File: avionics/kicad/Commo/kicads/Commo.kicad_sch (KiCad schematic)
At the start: 84 parts, among them U1 ByA 100nF +3V3 U1-VDDA Bypass, U1 ByB 100nF +3V3 U1-VDD Bypass

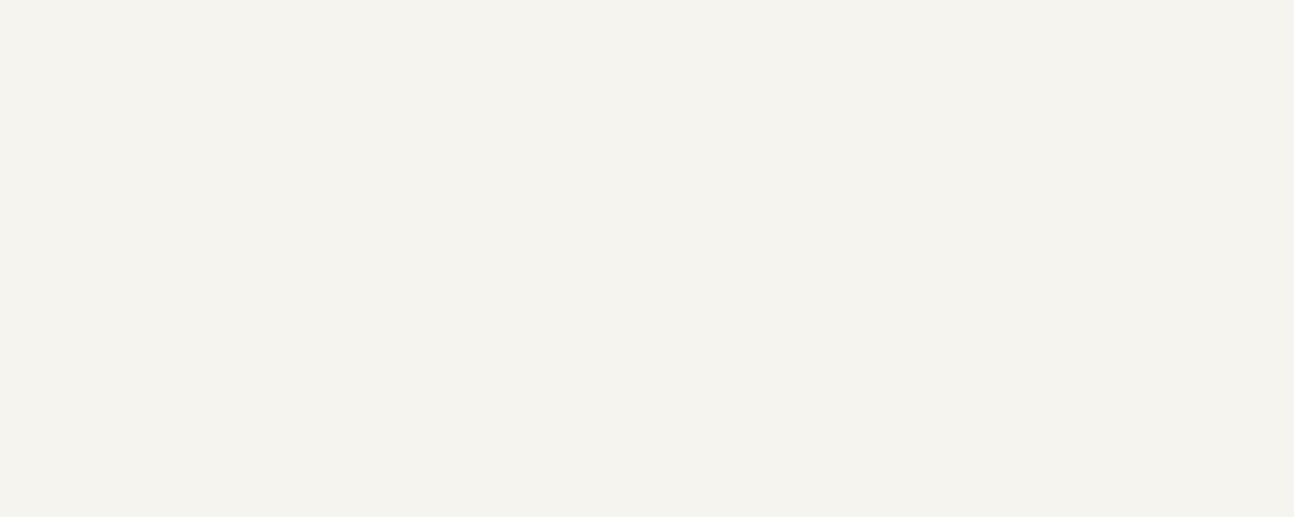
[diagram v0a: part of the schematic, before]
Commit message: docs(avionics): Wurth usage notice + uncrewed-only statement on 5 boards; catalogue REF-SENSOR-022..040
Owner decision 2026-09-26: retain the Wurth parts. The Wurth datasheet
usage notice is quoted verbatim [REF-SENSOR-028: Wurth 749010012A data
sheet rev 004.000 p.1] with an 'intended for use only on uncrewed
aircraft' statement in each Wurth-bearing board's .md, as a schematic
text item and PCB Cmts.User text, and in title-block comments 8/9
(tools/add_board_notices.py, idempotent). ERC/DRC/parity counts
unchanged on all five boards (kicad-cli 9.0.2).

REFERENCES.md: REF-SENSOR-022/023/025-030/033/038/040 were cited by
board schematics and generator scripts but never catalogued; entries
added with URLs validated 2026-09-26, unreachable ones marked
'requires verification'.

AI-authored: Claude Opus 5.5 (Anthropic).

Co-Authored-By: Claude Opus 5.5 <noreply@anthropic.com>
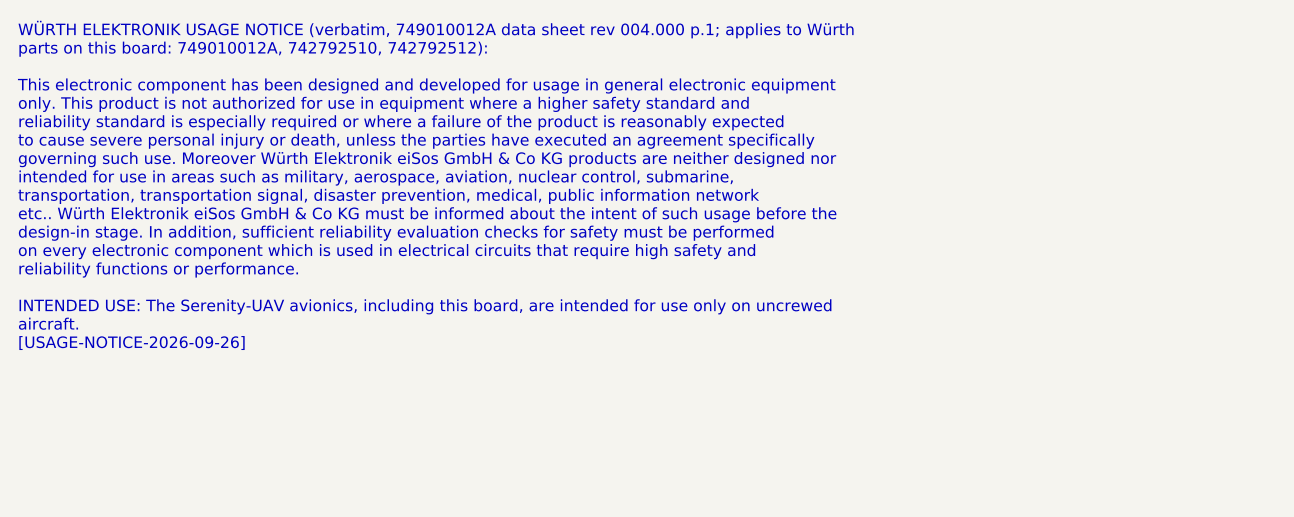
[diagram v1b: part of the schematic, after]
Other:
- note added: "WÜRTH ELEKTRONIK USAGE NOTICE (verbatim, 749010012A data sheet rev 004.000 p.1; applies to Würth parts on this board: 749010012A, 742792510, 742792512): This electronic component has been designed and developed for usage in general electronic equipment only. This product is not authorized for use in equipment where a higher safety standard and reliability standard is especially required or where 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"
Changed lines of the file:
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@@
     (comment 1 "Schematic-first reconciliation: authored to match Commo.kicad_pcb (J1 dropped; UART on PB2 rails; PTT_N + RSSI_DCD on gated payload GPIOs). 2026-09-21: LoRa (RFM95W) removed, replaced by SiK (RFD900ux-SMT) relocated from XO/TACCO -- see avionics/WBS.md sec1.2a.")
     (comment 2 "Author: Steve Griffing, PE(CSE), CISSP-ISSEP, CPP  |  AI-assist: Claude Opus 4.8 (Anthropic)")
-  )
+		(comment 8 "Wurth parts (749010012A, 742792510, 742792512): see Wurth usage notice on this page [USAGE-NOTICE-2026-09-26]")
+		(comment 9 "Intended for use ONLY on uncrewed aircraft")
+	)
   (text "POWER SUPPLY (5V input filter, MCP1703 LDO, bypass cascade)" (at 50.80 29.02 0) (effects (font (size 2.0 2.0) (bold yes)) (justify left)))
   (symbol (lib_id "Commo:S_+5V_Bead") (at 63.50 63.50 0) (unit 1)
@@
     (property "Intersheet References" "${INTERSHEET_REFS}" (at 229.87 1104.90 0)
       (effects (font (size 1.016 1.016)) (hide yes))))
-)
+	(text "WÜRTH ELEKTRONIK USAGE NOTICE (verbatim, 749010012A data sheet rev 004.000 p.1; applies to Würth\nparts on this board: 749010012A, 742792510, 742792512):\n\nThis electronic component has been designed and developed for usage in general electronic equipment\nonly. This product is not authorized for use in equipment where a higher safety standard and\nreliability standard is especially required or where a failure of the product is reasonably expected\nto cause severe personal injury or death, unless the parties have executed an agreement specifically\ngoverning such use. Moreover Würth Elektronik eiSos GmbH & Co KG products are neither designed nor\nintended for use in areas such as military, aerospace, aviation, nuclear control, submarine,\ntransportation, transportation signal, disaster prevention, medical, public information network\netc.. Würth Elektronik eiSos GmbH & Co KG must be informed about the intent of such usage before the\ndesign-in stage. In addition, sufficient reliability evaluation checks for safety must be performed\non every electronic component which is used in electrical circuits that require high safety and\nreliability functions or performance.\n\nINTENDED USE: The Serenity-UAV avionics, including this board, are intended for use only on uncrewed\naircraft.\n[USAGE-NOTICE-2026-09-26]"
+		(exclude_from_sim no)
+		(at -25.40 -88.90 0)
+		(effects (font (size 1.27 1.27)) (justify left top))
+	)
+	)

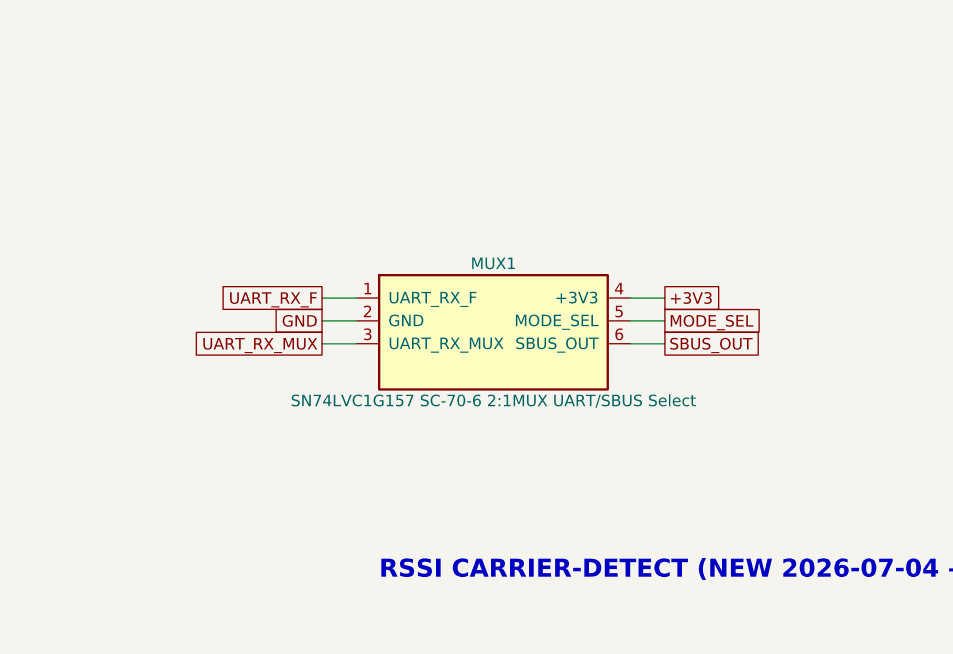
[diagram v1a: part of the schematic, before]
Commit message: fix(commo): MUX1 -> SN74LVC1G3157DRYR rewired per datasheet; add RF-ESD/BJT candidate datasheets
MUX1 had +3V3 on pin 4 and MODE_SEL on pin 5 (matches neither the '157
nor the '3157). Owner decision 2026-09-26: SN74LVC1G3157DRYR (USON-6,
1.45 x 1.0 mm), rewired per TI SCES424O (B1=UART_RX_F, B2=SBUS_OUT,
A=UART_RX_MUX, S=MODE_SEL, VCC=+3V3) via kicad_relink.py --rewire; GND
stitching via moved clear of the package. Commo ERC 0; parity 86 -> 85.

kicad_relink.py: --rewire mode; adds a missing Footprint property on the
instance (Commo instances had none, so parity saw an empty footprint).

Datasheets fetched for the antenna-TVS and PA-driver replacement
decisions: TI ESD501/601/701/801, Nexperia PESD5V0F1BL/PESD5V0X1BL,
Infineon ESD101-B1 (Rev 1.4), Nexperia PMBT2222A / MMBT2222A.

AI-authored: Claude Opus 5.5 (Anthropic).

Co-Authored-By: Claude Opus 5.5 <noreply@anthropic.com>
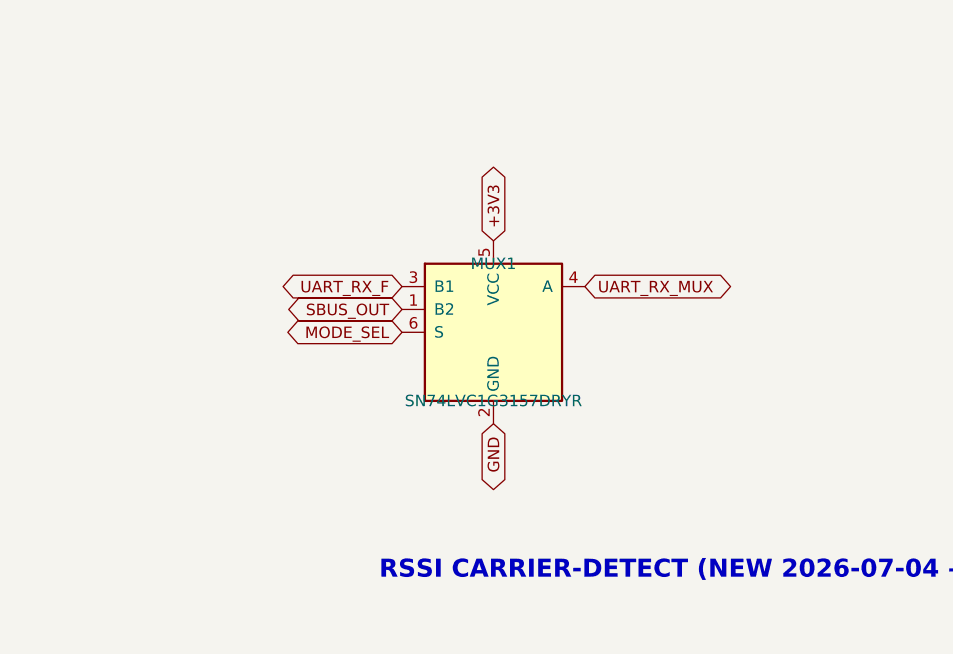
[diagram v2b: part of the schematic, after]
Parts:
- MUX1: value SN74LVC1G157 SC-70-6 2:1MUX UART/SBUS Select -> SN74LVC1G3157DRYR; footprint (none) -> Package_SON:Texas_USON-6_1x1.45mm_P0.5mm_SMD; symbol Commo:S_MUX1 -> SecureControllers:SN74LVC1G3157DRY
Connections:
- net +3V3: now also MUX1.5 (VCC); no longer MUX1.4 (+3V3)
- net MODE_SEL: now also MUX1.6 (S); no longer MUX1.5 (MODE_SEL)
- net SBUS_OUT: now also MUX1.1 (B2); no longer MUX1.6 (SBUS_OUT)
- net UART_RX_F: now also MUX1.3 (B1); no longer MUX1.1 (UART_RX_F)
- net UART_RX_MUX: now also MUX1.4 (A); no longer MUX1.3 (UART_RX_MUX)
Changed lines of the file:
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@@
   (global_label "+3V3" (shape passive) (at 558.80 730.25 0) (effects (font (size 1.27 1.27)) (justify left)))
   (no_connect (at 554.99 732.79))
-  (symbol (lib_id "Commo:S_MUX1") (at 63.50 795.02 0) (unit 1)
-    (exclude_from_sim no) (in_bom yes) (on_board yes) (dnp no)
+  (symbol (lib_id "SecureControllers:SN74LVC1G3157DRY") (at 63.50 795.02 0) (unit 1)
+    (exclude_from_sim no) (in_bom yes) (on_board yes) (dnp no)
+    (property "Footprint" "Package_SON:Texas_USON-6_1x1.45mm_P0.5mm_SMD" (at 63.50 795.02 0) (effects (font (size 1.27 1.27)) (hide yes)))
     (property "Reference" "MUX1" (at 63.50 787.40 0) (effects (font (size 1.27 1.27))))
-    (property "Value" "SN74LVC1G157  SC-70-6  2:1MUX  UART/SBUS Select" (at 63.50 802.64 0) (effects (font (size 1.27 1.27))))
+    (property "Value" "SN74LVC1G3157DRYR" (at 63.50 802.64 0) (effects (font (size 1.27 1.27))))
     (pin "1")
     (pin "2")
@@
     (instances (project "Commo" (path "/49030000-0000-0000-0000-000000000001" (reference "MUX1") (unit 1))))
   )
-  (wire (pts (xy 48.26 791.21) (xy 44.45 791.21)) (stroke (width 0) (type default)))
-  (global_label "UART_RX_F" (shape passive) (at 44.45 791.21 180) (effects (font (size 1.27 1.27)) (justify right)))
-  (wire (pts (xy 48.26 793.75) (xy 44.45 793.75)) (stroke (width 0) (type default)))
-  (global_label "GND" (shape passive) (at 44.45 793.75 180) (effects (font (size 1.27 1.27)) (justify right)))
-  (wire (pts (xy 48.26 796.29) (xy 44.45 796.29)) (stroke (width 0) (type default)))
-  (global_label "UART_RX_MUX" (shape passive) (at 44.45 796.29 180) (effects (font (size 1.27 1.27)) (justify right)))
-  (wire (pts (xy 78.74 791.21) (xy 82.55 791.21)) (stroke (width 0) (type default)))
-  (global_label "+3V3" (shape passive) (at 82.55 791.21 0) (effects (font (size 1.27 1.27)) (justify left)))
-  (wire (pts (xy 78.74 793.75) (xy 82.55 793.75)) (stroke (width 0) (type default)))
-  (global_label "MODE_SEL" (shape passive) (at 82.55 793.75 0) (effects (font (size 1.27 1.27)) (justify left)))
-  (wire (pts (xy 78.74 796.29) (xy 82.55 796.29)) (stroke (width 0) (type default)))
-  (global_label "SBUS_OUT" (shape passive) (at 82.55 796.29 0) (effects (font (size 1.27 1.27)) (justify left)))
   (symbol (lib_id "Commo:S_S1") (at 158.75 795.02 0) (unit 1)
     (exclude_from_sim no) (in_bom yes) (on_board yes) (dnp no)
@@
 		(effects (font (size 1.27 1.27)) (justify left top))
 	)
-	)
+	(global_label "UART_RX_F" (shape bidirectional) (at 53.3400 789.9400 180)
+    (effects (font (size 1.27 1.27)))
+)
+  (global_label "SBUS_OUT" (shape bidirectional) (at 53.3400 792.4800 180)
+    (effects (font (size 1.27 1.27)))
+)
+  (global_label "UART_RX_MUX" (shape bidirectional) (at 73.6600 789.9400 0)
+    (effects (font (size 1.27 1.27)))
+)
+  (global_label "MODE_SEL" (shape bidirectional) (at 53.3400 795.0200 180)
+    (effects (font (size 1.27 1.27)))
+)
+  (global_label "+3V3" (shape bidirectional) (at 63.5000 784.8600 90)
+    (effects (font (size 1.27 1.27)))
+)
+  (global_label "GND" (shape bidirectional) (at 63.5000 805.1800 270)
+    (effects (font (size 1.27 1.27)))
+)
+  )

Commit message: fix(avionics): antenna TVS -> ESD101-B1-02ELS, PA driver -> PMBT2222A; atomic + back-side relink
Owner decisions 2026-09-26 (avionics/WBS.md U7.1j):
- TACCO D-ANT-WIOE5 / D-ANT-RADIO and Commo D-ANT-SIK: deprecated
  RCLAMP0502B -> Infineon ESD101-B1-02ELS (0.1 pF, TSSLP-2-4). The
  proposed RClamp0504FA (3 pF) was rejected for 50-ohm antenna ports
  (0.7 dB at 915 MHz, 3.7-8.8 dB at 2.4/5 GHz). D-ANT-SIK relocated
  beside J-ANT-SIK (old pad 1 overlapped the MH3 hole).
- Commo PA Drvr: MMBT2222A -> Nexperia PMBT2222A (same pinout).
- TACCO.md / Commo.md RF-ESD and BOM text rewritten; unverified 0.15 pF
  RCLAMP claim removed.
- kicad_relink.py: writes schematic and PCB only if both edits succeed;
  supports back-side footprints (local y mirrored, F->B layers).
TACCO: ERC 0, parity 0. Commo: ERC 0, parity 85 -> 83.

AI-authored: Claude Opus 5.5 (Anthropic).

Co-Authored-By: Claude Opus 5.5 <noreply@anthropic.com>
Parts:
- D-ANT-SIK: value RCLAMP0502B -> ESD101-B1-02ELS; footprint (none) -> SecureControllers:Infineon_TSSLP-2-4_0.62x0.32mm; symbol Commo:S_D_ANT_SIK -> SecureControllers:ESD101-B1-02ELS
- PA Drvr: value MMBT2222A NPN BJT PA Class-A Driver -> PMBT2222A,215; footprint (none) -> Package_TO_SOT_SMD:SOT-23; symbol Commo:S_PA_Drvr -> SecureControllers:PMBT2222A
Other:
- moved on the sheet: PA Drvr
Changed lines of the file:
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@@
   (wire (pts (xy 173.99 245.11) (xy 177.80 245.11)) (stroke (width 0) (type default)))
   (global_label "PA_INT" (shape passive) (at 177.80 245.11 0) (effects (font (size 1.27 1.27)) (justify left)))
-  (symbol (lib_id "Commo:S_PA_Drvr") (at 254.00 246.38 0) (unit 1)
-    (exclude_from_sim no) (in_bom yes) (on_board yes) (dnp no)
+  (symbol (lib_id "SecureControllers:PMBT2222A") (at 254.00 246.38 0) (unit 1)
+    (exclude_from_sim no) (in_bom yes) (on_board yes) (dnp no)
+    (property "Datasheet" "https://assets.nexperia.com/documents/data-sheet/PMBT2222A.pdf" (at 254.00 246.38 0) (effects (font (size 1.27 1.27)) (hide yes)))
+    (property "Footprint" "Package_TO_SOT_SMD:SOT-23" (at 254.00 246.38 0) (effects (font (size 1.27 1.27)) (hide yes)))
     (property "Reference" "PA Drvr" (at 254.00 240.03 0) (effects (font (size 1.27 1.27))))
-    (property "Value" "MMBT2222A  NPN BJT  PA Class-A Driver" (at 254.00 252.73 0) (effects (font (size 1.27 1.27))))
+    (property "Value" "PMBT2222A,215" (at 254.00 252.73 0) (effects (font (size 1.27 1.27))))
     (pin "1")
     (pin "2")
@@
     (instances (project "Commo" (path "/49030000-0000-0000-0000-000000000001" (reference "PA Drvr") (unit 1))))
   )
-  (wire (pts (xy 238.76 243.84) (xy 234.95 243.84)) (stroke (width 0) (type default)))
-  (global_label "DDS_RF" (shape passive) (at 234.95 243.84 180) (effects (font (size 1.27 1.27)) (justify right)))
-  (wire (pts (xy 238.76 246.38) (xy 234.95 246.38)) (stroke (width 0) (type default)))
-  (global_label "GND" (shape passive) (at 234.95 246.38 180) (effects (font (size 1.27 1.27)) (justify right)))
-  (wire (pts (xy 269.24 243.84) (xy 273.05 243.84)) (stroke (width 0) (type default)))
-  (global_label "PA_INT" (shape passive) (at 273.05 243.84 0) (effects (font (size 1.27 1.27)) (justify left)))
   (symbol (lib_id "Commo:S_PA_Rc1") (at 349.25 246.38 0) (unit 1)
     (exclude_from_sim no) (in_bom yes) (on_board yes) (dnp no)
@@
   (wire (pts (xy 78.74 1198.88) (xy 82.55 1198.88)) (stroke (width 0) (type default)))
   (global_label "GND" (shape passive) (at 82.55 1198.88 0) (effects (font (size 1.27 1.27)) (justify left)))
-  (symbol (lib_id "Commo:S_D_ANT_SIK") (at 63.50 1212.85 0) (unit 1)
-    (exclude_from_sim no) (in_bom yes) (on_board yes) (dnp no)
+  (symbol (lib_id "SecureControllers:ESD101-B1-02ELS") (at 63.50 1212.85 0) (unit 1)
+    (exclude_from_sim no) (in_bom yes) (on_board yes) (dnp no)
+    (property "Datasheet" "https://www.infineon.com/assets/row/public/documents/24/49/infineon-esd101-b1-datasheet-en.pdf" (at 63.50 1212.85 0) (effects (font (size 1.27 1.27)) (hide yes)))
+    (property "Footprint" "SecureControllers:Infineon_TSSLP-2-4_0.62x0.32mm" (at 63.50 1212.85 0) (effects (font (size 1.27 1.27)) (hide yes)))
     (property "Reference" "D-ANT-SIK" (at 63.50 1206.50 0) (effects (font (size 1.27 1.27))))
-    (property "Value" "RCLAMP0502B" (at 63.50 1219.20 0) (effects (font (size 1.27 1.27))))
+    (property "Value" "ESD101-B1-02ELS" (at 63.50 1219.20 0) (effects (font (size 1.27 1.27))))
     (pin "1")
     (pin "2")
     (instances (project "Commo" (path "/49030000-0000-0000-0000-000000000001" (reference "D-ANT-SIK") (unit 1))))
   )
-  (wire (pts (xy 48.26 1211.58) (xy 44.45 1211.58)) (stroke (width 0) (type default)))
-  (global_label "SIK_ANT_F" (shape passive) (at 44.45 1211.58 180) (effects (font (size 1.27 1.27)) (justify right)))
-  (wire (pts (xy 78.74 1211.58) (xy 82.55 1211.58)) (stroke (width 0) (type default)))
-  (global_label "GND" (shape passive) (at 82.55 1211.58 0) (effects (font (size 1.27 1.27)) (justify left)))
   (symbol (lib_id "Commo:S_J_ANT_SIK") (at 101.60 1225.55 0) (unit 1)
     (exclude_from_sim no) (in_bom yes) (on_board yes) (dnp no)
@@
     (effects (font (size 1.27 1.27)))
 )
+  (global_label "SIK_ANT_F" (shape bidirectional) (at 63.5000 1202.6900 90)
+    (effects (font (size 1.27 1.27)))
+)
+  (global_label "GND" (shape bidirectional) (at 63.5000 1223.0100 270)
+    (effects (font (size 1.27 1.27)))
+)
+  (global_label "DDS_RF" (shape bidirectional) (at 243.8400 241.3000 180)
+    (effects (font (size 1.27 1.27)))
+)
+  (global_label "GND" (shape bidirectional) (at 254.0000 256.5400 270)
+    (effects (font (size 1.27 1.27)))
+)
+  (global_label "PA_INT" (shape bidirectional) (at 254.0000 236.2200 90)
+    (effects (font (size 1.27 1.27)))
+)
